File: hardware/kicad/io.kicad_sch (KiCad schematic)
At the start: 7 parts, among them U10 UART_USB, U11 74AC138, U12 SC16C752, U13 W65C22S

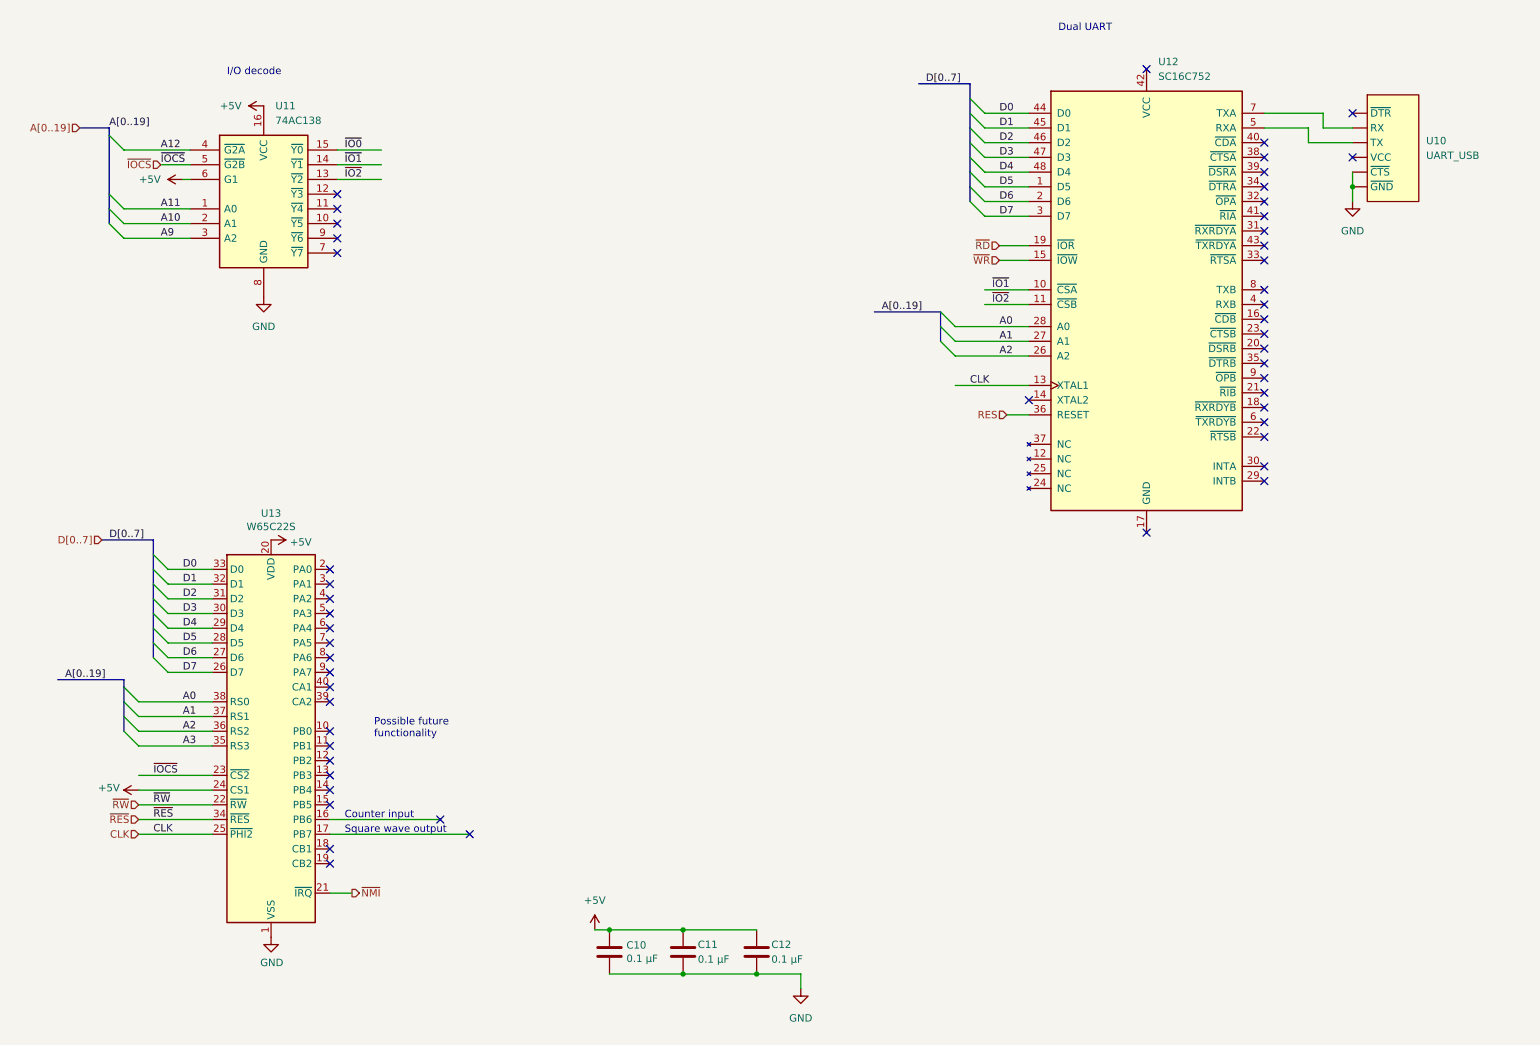
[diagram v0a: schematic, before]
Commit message: update hardware files to match current WIP design
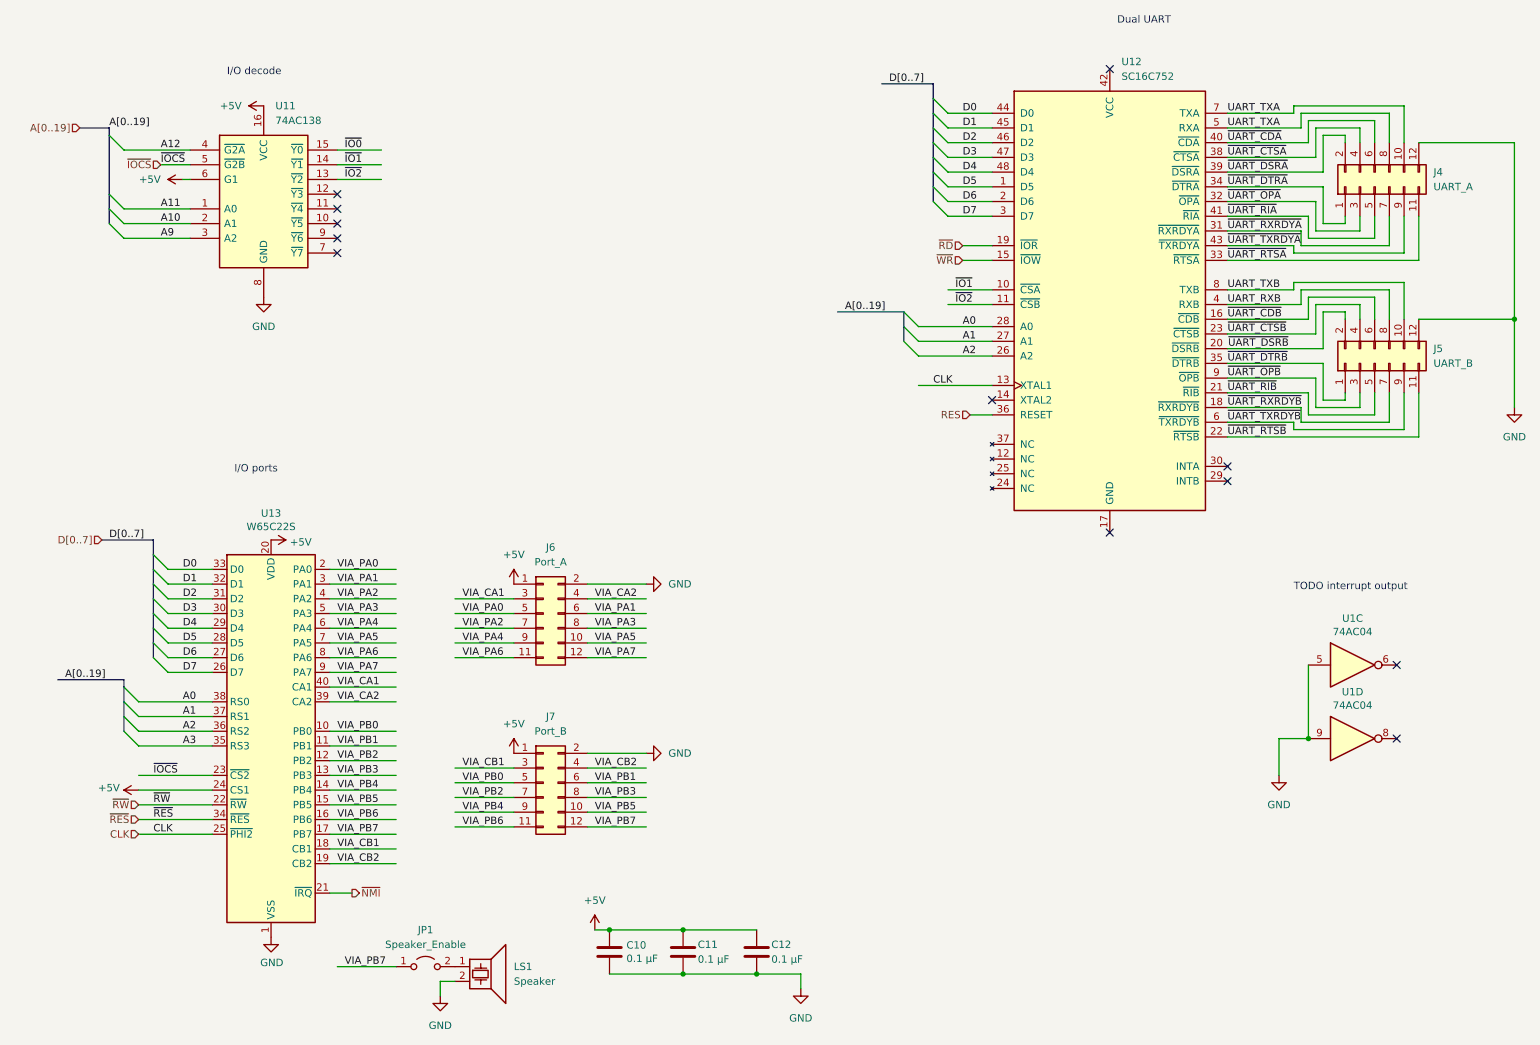
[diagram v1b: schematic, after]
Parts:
- removed U10: UART_USB, symbol project:UART_USB
- added J4: UART_A, Connector_PinHeader_2.54mm:PinHeader_2x06_P2.54mm_Vertical, symbol Connector_Generic:Conn_02x06_Odd_Even
- added J5: UART_B, Connector_PinHeader_2.54mm:PinHeader_2x06_P2.54mm_Vertical, symbol Connector_Generic:Conn_02x06_Odd_Even
- added J6: Port_A, Connector_PinHeader_2.54mm:PinHeader_2x06_P2.54mm_Vertical, symbol Connector_Generic:Conn_02x06_Odd_Even
- added J7: Port_B, Connector_PinHeader_2.54mm:PinHeader_2x06_P2.54mm_Vertical, symbol Connector_Generic:Conn_02x06_Odd_Even
- added JP1: Speaker_Enable, Connector_PinHeader_2.54mm:PinHeader_1x02_P2.54mm_Vertical, symbol Jumper:Jumper_2_Open
- added LS1: Speaker, Buzzer_Beeper:Buzzer_TDK_PS1240P02BT_D12.2mm_H6.5mm, symbol Device:Speaker_Crystal
- added U1: 74AC04, Package_DIP:DIP-14_W7.62mm_Socket, symbol project:74AC04
- C10, C11, C12: footprint (none) -> Capacitor_SMD:C_0603_1608Metric_Pad1.08x0.95mm_HandSolder
- U11: footprint (none) -> Package_DIP:DIP-16_W7.62mm_Socket
- U12: footprint (none) -> Package_QFP:LQFP-48_7x7mm_P0.5mm
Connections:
- net +5V: now also J6.1 (Pin_1), J7.1 (Pin_1)
- net GND: now also J4.12 (Pin_12), J5.12 (Pin_12), J6.2 (Pin_2), J7.2 (Pin_2), LS1.2, U1.5, U1.9
- net UART_TXA: now reaches U12.5 (RXA)
- net UART_TXA: now also U12.7 (TXA), J4.10 (Pin_10), J4.8 (Pin_8)
- net ~{UART_CDB}: now reaches U12.16 (~{CDB})
- net ~{UART_CDB}: now also J5.6 (Pin_6)
- net ~{UART_RXRDYB}: now reaches U12.18 (~{RXRDYB})
- net ~{UART_RXRDYB}: now also J5.7 (Pin_7)
- net ~{UART_DSRB}: now reaches U12.20 (~{DSRB})
- net ~{UART_DSRB}: now also J5.2 (Pin_2)
- net ~{UART_RIB}: now reaches U12.21 (~{RIB})
- net ~{UART_RIB}: now also J5.5 (Pin_5)
- net ~{UART_RTSB}: now reaches U12.22 (~{RTSB})
- net ~{UART_RTSB}: now also J5.11 (Pin_11)
- net ~{UART_CTSB}: now reaches U12.23 (~{CTSB})
- net ~{UART_CTSB}: now also J5.4 (Pin_4)
- net ~{UART_RXRDYA}: now reaches U12.31 (~{RXRDYA})
- net ~{UART_RXRDYA}: now also J4.7 (Pin_7)
- net ~{UART_OPA}: now reaches U12.32 (~{OPA})
- net ~{UART_OPA}: now also J4.3 (Pin_3)
- net ~{UART_RTSA}: now reaches U12.33 (~{RTSA})
- net ~{UART_RTSA}: now also J4.11 (Pin_11)
- net ~{UART_DTRA}: now reaches U12.34 (~{DTRA})
- net ~{UART_DTRA}: now also J4.1 (Pin_1)
- net ~{UART_DTRB}: now reaches U12.35 (~{DTRB})
- net ~{UART_DTRB}: now also J5.1 (Pin_1)
- net ~{UART_CTSA}: now reaches U12.38 (~{CTSA})
- net ~{UART_CTSA}: now also J4.4 (Pin_4)
- net ~{UART_DSRA}: now reaches U12.39 (~{DSRA})
- net ~{UART_DSRA}: now also J4.2 (Pin_2)
- net UART_RXB: now reaches U12.4 (RXB)
- net UART_RXB: now also J5.8 (Pin_8)
- net ~{UART_CDA}: now reaches U12.40 (~{CDA})
- net ~{UART_CDA}: now also J4.6 (Pin_6)
- net ~{UART_RIA}: now reaches U12.41 (~{RIA})
- net ~{UART_RIA}: now also J4.5 (Pin_5)
- net ~{UART_TXRDYA}: now reaches U12.43 (~{TXRDYA})
- net ~{UART_TXRDYA}: now also J4.9 (Pin_9)
- net ~{UART_TXRDYB}: now reaches U12.6 (~{TXRDYB})
- net ~{UART_TXRDYB}: now also J5.9 (Pin_9)
- net UART_TXB: now reaches U12.8 (TXB)
- net UART_TXB: now also J5.10 (Pin_10)
- net ~{UART_OPB}: now reaches U12.9 (~{OPB})
- net ~{UART_OPB}: now also J5.3 (Pin_3)
- net VIA_PB0: now reaches U13.10 (PB0)
- net VIA_PB0: now also J7.5 (Pin_5)
- net VIA_PB1: now reaches U13.11 (PB1)
- net VIA_PB1: now also J7.6 (Pin_6)
- net VIA_PB2: now reaches U13.12 (PB2)
- net VIA_PB2: now also J7.7 (Pin_7)
- net VIA_PB3: now reaches U13.13 (PB3)
- net VIA_PB3: now also J7.8 (Pin_8)
- net VIA_PB4: now reaches U13.14 (PB4)
- net VIA_PB4: now also J7.9 (Pin_9)
- net VIA_PB5: now reaches U13.15 (PB5)
- net VIA_PB5: now also J7.10 (Pin_10)
- net VIA_PB6: now reaches U13.16 (PB6)
- net VIA_PB6: now also J7.11 (Pin_11)
- net VIA_PB7: now reaches U13.17 (PB7)
- net VIA_PB7: now also J7.12 (Pin_12), JP1.1 (A)
- net VIA_CB1: now reaches U13.18 (CB1)
- net VIA_CB1: now also J7.3 (Pin_3)
- net VIA_CB2: now reaches U13.19 (CB2)
- net VIA_CB2: now also J7.4 (Pin_4)
- net VIA_PA0: now reaches U13.2 (PA0)
- net VIA_PA0: now also J6.5 (Pin_5)
- net VIA_PA1: now reaches U13.3 (PA1)
- net VIA_PA1: now also J6.6 (Pin_6)
- net VIA_CA2: now reaches U13.39 (CA2)
- net VIA_CA2: now also J6.4 (Pin_4)
- net VIA_PA2: now reaches U13.4 (PA2)
- net VIA_PA2: now also J6.7 (Pin_7)
- net VIA_CA1: now reaches U13.40 (CA1)
- net VIA_CA1: now also J6.3 (Pin_3)
- net VIA_PA3: now reaches U13.5 (PA3)
- net VIA_PA3: now also J6.8 (Pin_8)
- net VIA_PA4: now reaches U13.6 (PA4)
- net VIA_PA4: now also J6.9 (Pin_9)
- net VIA_PA5: now reaches U13.7 (PA5)
- net VIA_PA5: now also J6.10 (Pin_10)
- net VIA_PA6: now reaches U13.8 (PA6)
- net VIA_PA6: now also J6.11 (Pin_11)
- net VIA_PA7: now reaches U13.9 (PA7)
- net VIA_PA7: now also J6.12 (Pin_12)
- new net: JP1.2 (B), LS1.1
- no-connect marks 52 -> 12
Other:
- note added: "I/O ports"
- note added: "TODO interrupt output"
- note removed: "Counter input"
- note removed: "Possible future functionality"
- note removed: "Square wave output"
- moved on the sheet: U12
